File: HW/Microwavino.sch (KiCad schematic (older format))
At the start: 56 parts, among them P1 SMA, P2 SMA, P3 SMA, P4 SMA, U1 MIC5366, U2 MCP1824T, U3 MCP1824T, U4 MCP1824T, U5 ASTXR-12-19.200MHz, U6 MAX2871, U7 Teensy3.2

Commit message: testing connection
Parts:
- added R?: 5.1k, Resistors_SMD:R_0402, symbol R
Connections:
- net 3V3_DIG: now also R?.1
- net CE: now also R?.2
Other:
- note added: "Fast Lock Circuit\n(may be omitted)"
- note added: "Loop Filter"

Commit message: prelim placement
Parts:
- C10, C11, C12, C13, C14, C15, C16, C17, C18, C19, C20, C21, C22, C23, C24, C25, C28, C9: footprint Capacitors_SMD:C_0402 -> VNA:C_0402b
- D1: footprint (none) -> VNA:LED_0603
- R1, R10, R11, R2, R3, R4, R5, R6, R7, R8, R9: footprint Resistors_SMD:R_0402 -> VNA:R_0402b
- R12: renamed from R?; footprint Resistors_SMD:R_0402 -> VNA:R_0402b
- U1: footprint TO_SOT_Packages_SMD:SOT-353_SC-70-5 -> VNA:SOT-23-5
- U7: footprint kicad_teensy-master:Teensy30_31_32_LC -> VNA:Teensy30_31_32_LC_modified
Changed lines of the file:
@@
 F 0 "C12" H 5225 7600 50  0000 L CNN
 F 1 "1u" H 5225 7400 50  0000 L CNN
-F 2 "Capacitors_SMD:C_0402" H 5238 7350 30  0001 C CNN
+F 2 "VNA:C_0402b" H 5238 7350 30  0001 C CNN
 F 3 "" H 5200 7500 60  0000 C CNN
 	1    5200 7500
@@
 F 0 "C10" H 5025 7600 50  0000 L CNN
 F 1 "1u" H 5025 7400 50  0000 L CNN
-F 2 "Capacitors_SMD:C_0402" H 5038 7350 30  0001 C CNN
+F 2 "VNA:C_0402b" H 5038 7350 30  0001 C CNN
 F 3 "" H 5000 7500 60  0000 C CNN
 	1    5000 7500
@@
 F 0 "C9" H 4825 7600 50  0000 L CNN
 F 1 "1u" H 4825 7400 50  0000 L CNN
-F 2 "Capacitors_SMD:C_0402" H 4838 7350 30  0001 C CNN
+F 2 "VNA:C_0402b" H 4838 7350 30  0001 C CNN
 F 3 "" H 4800 7500 60  0000 C CNN
 	1    4800 7500
@@
 F 0 "R1" V 4680 7500 50  0000 C CNN
 F 1 "5.1k" V 4600 7500 50  0000 C CNN
-F 2 "Resistors_SMD:R_0402" V 4530 7500 30  0001 C CNN
+F 2 "VNA:R_0402b" V 4530 7500 30  0001 C CNN
 F 3 "" H 4600 7500 30  0000 C CNN
 	1    4600 7500
@@
 F 0 "C24" H 8725 6950 50  0000 L CNN
 F 1 "820p" H 8725 6750 50  0000 L CNN
-F 2 "Capacitors_SMD:C_0402" H 8738 6700 30  0001 C CNN
+F 2 "VNA:C_0402b" H 8738 6700 30  0001 C CNN
 F 3 "" H 8700 6850 60  0000 C CNN
 	1    8700 6850
@@
 F 0 "R5" V 9130 6700 50  0000 C CNN
 F 1 "240" V 9050 6700 50  0000 C CNN
-F 2 "Resistors_SMD:R_0402" V 8980 6700 30  0001 C CNN
+F 2 "VNA:R_0402b" V 8980 6700 30  0001 C CNN
 F 3 "" H 9050 6700 30  0000 C CNN
 	1    9050 6700
@@
 F 0 "C23" H 8725 6400 50  0000 L CNN
 F 1 "12n" H 8725 6200 50  0000 L CNN
-F 2 "Capacitors_SMD:C_0402" H 8738 6150 30  0001 C CNN
+F 2 "VNA:C_0402b" H 8738 6150 30  0001 C CNN
 F 3 "" H 8700 6300 60  0000 C CNN
 	1    8700 6300
@@
 F 0 "C22" H 8725 6050 50  0000 L CNN
 F 1 "100n" H 8725 5850 50  0000 L CNN
-F 2 "Capacitors_SMD:C_0402" H 8738 5800 30  0001 C CNN
+F 2 "VNA:C_0402b" H 8738 5800 30  0001 C CNN
 F 3 "" H 8700 5950 60  0000 C CNN
 	1    8700 5950
@@
 F 0 "R4" V 8580 5800 50  0000 C CNN
 F 1 "30.1" V 8500 5800 50  0000 C CNN
-F 2 "Resistors_SMD:R_0402" V 8430 5800 30  0001 C CNN
+F 2 "VNA:R_0402b" V 8430 5800 30  0001 C CNN
 F 3 "" H 8500 5800 30  0000 C CNN
 	1    8500 5800
@@
 F 0 "R3" V 8380 5950 50  0000 C CNN
 F 1 "90.9" V 8300 5950 50  0000 C CNN
-F 2 "Resistors_SMD:R_0402" V 8230 5950 30  0001 C CNN
+F 2 "VNA:R_0402b" V 8230 5950 30  0001 C CNN
 F 3 "" H 8300 5950 30  0000 C CNN
 	1    8300 5950
@@
 F 0 "C25" H 10575 6450 50  0000 L CNN
 F 1 "100p" H 10575 6250 50  0000 L CNN
-F 2 "Capacitors_SMD:C_0402" H 10588 6200 30  0001 C CNN
+F 2 "VNA:C_0402b" H 10588 6200 30  0001 C CNN
 F 3 "" H 10550 6350 60  0000 C CNN
 	1    10550 6350
@@
 F 0 "C17" H 5725 4450 50  0000 L CNN
 F 1 "100n" H 5725 4250 50  0000 L CNN
-F 2 "Capacitors_SMD:C_0402" H 5738 4200 30  0001 C CNN
+F 2 "VNA:C_0402b" H 5738 4200 30  0001 C CNN
 F 3 "" H 5700 4350 60  0000 C CNN
 	1    5700 4350
@@
 F 0 "C20" H 5975 4450 50  0000 L CNN
 F 1 "100p" H 5975 4250 50  0000 L CNN
-F 2 "Capacitors_SMD:C_0402" H 5988 4200 30  0001 C CNN
+F 2 "VNA:C_0402b" H 5988 4200 30  0001 C CNN
 F 3 "" H 5950 4350 60  0000 C CNN
 	1    5950 4350
@@
 F 0 "C18" H 5725 5200 50  0000 L CNN
 F 1 "100n" H 5725 5000 50  0000 L CNN
-F 2 "Capacitors_SMD:C_0402" H 5738 4950 30  0001 C CNN
+F 2 "VNA:C_0402b" H 5738 4950 30  0001 C CNN
 F 3 "" H 5700 5100 60  0000 C CNN
 	1    5700 5100
@@
 F 0 "C21" H 5975 5200 50  0000 L CNN
 F 1 "100p" H 5975 5000 50  0000 L CNN
-F 2 "Capacitors_SMD:C_0402" H 5988 4950 30  0001 C CNN
+F 2 "VNA:C_0402b" H 5988 4950 30  0001 C CNN
 F 3 "" H 5950 5100 60  0000 C CNN
 	1    5950 5100
@@
 F 0 "C14" H 5475 4450 50  0000 L CNN
 F 1 "100n" H 5475 4250 50  0000 L CNN
-F 2 "Capacitors_SMD:C_0402" H 5488 4200 30  0001 C CNN
+F 2 "VNA:C_0402b" H 5488 4200 30  0001 C CNN
 F 3 "" H 5450 4350 60  0000 C CNN
 	1    5450 4350
@@
 F 0 "C15" H 5475 5200 50  0000 L CNN
 F 1 "100n" H 5475 5000 50  0000 L CNN
-F 2 "Capacitors_SMD:C_0402" H 5488 4950 30  0001 C CNN
+F 2 "VNA:C_0402b" H 5488 4950 30  0001 C CNN
 F 3 "" H 5450 5100 60  0000 C CNN
 	1    5450 5100
@@
 F 0 "R8" V 11080 6450 50  0000 C CNN
 F 1 "49.9" V 11000 6450 50  0000 C CNN
-F 2 "Resistors_SMD:R_0402" V 10930 6450 30  0001 C CNN
+F 2 "VNA:R_0402b" V 10930 6450 30  0001 C CNN
 F 3 "" H 11000 6450 30  0000 C CNN
 	1    11000 6450
@@
 F 0 "C11" V 5000 6050 50  0000 L CNN
 F 1 "10n" V 5100 6050 50  0000 L CNN
-F 2 "Capacitors_SMD:C_0402" H 5088 5800 30  0001 C CNN
+F 2 "VNA:C_0402b" H 5088 5800 30  0001 C CNN
 F 3 "" H 5050 5950 60  0000 C CNN
 	1    5050 5950
@@
 F 0 "U1" H 3250 5800 60  0000 C CNN
 F 1 "MIC5366" H 3100 6200 60  0000 C CNN
-F 2 "TO_SOT_Packages_SMD:SOT-353_SC-70-5" H 3050 5850 60  0001 C CNN
+F 2 "VNA:SOT-23-5" H 3050 5850 60  0001 C CNN
 F 3 "" H 3050 5850 60  0000 C CNN
 	1    3100 6000
@@
 F 0 "U7" H 11400 4650 60  0000 C CNN
 F 1 "Teensy3.2" H 11400 1650 60  0000 C CNN
-F 2 "kicad_teensy-master:Teensy30_31_32_LC" H 11400 2350 60  0001 C CNN
+F 2 "VNA:Teensy30_31_32_LC_modified" H 11400 2350 60  0001 C CNN
 F 3 "" H 11400 2350 60  0000 C CNN
 	1    11400 3150
@@
 F 0 "C16" H 5725 3650 50  0000 L CNN
 F 1 "100n" H 5725 3450 50  0000 L CNN
-F 2 "Capacitors_SMD:C_0402" H 5738 3400 30  0001 C CNN
+F 2 "VNA:C_0402b" H 5738 3400 30  0001 C CNN
 F 3 "" H 5700 3550 60  0000 C CNN
 	1    5700 3550
@@
 F 0 "C19" H 5975 3650 50  0000 L CNN
 F 1 "100p" H 5975 3450 50  0000 L CNN
-F 2 "Capacitors_SMD:C_0402" H 5988 3400 30  0001 C CNN
+F 2 "VNA:C_0402b" H 5988 3400 30  0001 C CNN
 F 3 "" H 5950 3550 60  0000 C CNN
 	1    5950 3550
@@
 F 0 "C13" H 5475 3650 50  0000 L CNN
 F 1 "100n" H 5475 3450 50  0000 L CNN
-F 2 "Capacitors_SMD:C_0402" H 5488 3400 30  0001 C CNN
+F 2 "VNA:C_0402b" H 5488 3400 30  0001 C CNN
 F 3 "" H 5450 3550 60  0000 C CNN
 	1    5450 3550
@@
 F 0 "R6" V 10880 7100 50  0000 C CNN
 F 1 "49.9" V 10800 7100 50  0000 C CNN
-F 2 "Resistors_SMD:R_0402" V 10730 7100 30  0001 C CNN
+F 2 "VNA:R_0402b" V 10730 7100 30  0001 C CNN
 F 3 "" H 10800 7100 30  0000 C CNN
 	1    10800 7100
@@
 F 0 "C28" H 12475 6450 50  0000 L CNN
 F 1 "100p" H 12475 6250 50  0000 L CNN
-F 2 "Capacitors_SMD:C_0402" H 12488 6200 30  0001 C CNN
+F 2 "VNA:C_0402b" H 12488 6200 30  0001 C CNN
 F 3 "" H 12450 6350 60  0000 C CNN
 	1    12450 6350
@@
 F 0 "R11" V 12980 6450 50  0000 C CNN
 F 1 "49.9" V 12900 6450 50  0000 C CNN
-F 2 "Resistors_SMD:R_0402" V 12830 6450 30  0001 C CNN
+F 2 "VNA:R_0402b" V 12830 6450 30  0001 C CNN
 F 3 "" H 12900 6450 30  0000 C CNN
 	1    12900 6450
@@
 F 0 "R9" V 12780 7100 50  0000 C CNN
 F 1 "49.9" V 12700 7100 50  0000 C CNN
-F 2 "Resistors_SMD:R_0402" V 12630 7100 30  0001 C CNN
+F 2 "VNA:R_0402b" V 12630 7100 30  0001 C CNN
 F 3 "" H 12700 7100 30  0000 C CNN
 	1    12700 7100
@@
 F 0 "R7" V 10880 7800 50  0000 C CNN
 F 1 "49.9" V 10800 7800 50  0000 C CNN
-F 2 "Resistors_SMD:R_0402" V 10730 7800 30  0001 C CNN
+F 2 "VNA:R_0402b" V 10730 7800 30  0001 C CNN
 F 3 "" H 10800 7800 30  0000 C CNN
 	1    10800 7800
@@
 F 0 "R10" V 12780 7800 50  0000 C CNN
 F 1 "49.9" V 12700 7800 50  0000 C CNN
-F 2 "Resistors_SMD:R_0402" V 12630 7800 30  0001 C CNN
+F 2 "VNA:R_0402b" V 12630 7800 30  0001 C CNN
 F 3 "" H 12700 7800 30  0000 C CNN
 	1    12700 7800
@@
 F 0 "D1" H 7400 5525 50  0000 L CNN
 F 1 "LED_Small_ALT" H 7275 5300 50  0001 L CNN
-F 2 "" V 7450 5400 50  0001 C CNN
+F 2 "VNA:LED_0603" V 7450 5400 50  0001 C CNN
 F 3 "" V 7450 5400 50  0001 C CNN
 	1    7450 5400
@@
 F 0 "R2" V 7530 5700 50  0000 C CNN
 F 1 "240" V 7450 5700 50  0000 C CNN
-F 2 "Resistors_SMD:R_0402" V 7380 5700 30  0001 C CNN
+F 2 "VNA:R_0402b" V 7380 5700 30  0001 C CNN
 F 3 "" H 7450 5700 30  0000 C CNN
 	1    7450 5700
@@
 Fast Lock Circuit\n(may be omitted)
 $Comp
-L R R?
+L R R12
 U 1 1 59B1334E
 P 3750 7300
-F 0 "R?" V 3830 7300 50  0000 C CNN
+F 0 "R12" V 3830 7300 50  0000 C CNN
 F 1 "5.1k" V 3750 7300 50  0000 C CNN
-F 2 "Resistors_SMD:R_0402" V 3680 7300 30  0001 C CNN
+F 2 "VNA:R_0402b" V 3680 7300 30  0001 C CNN
 F 3 "" H 3750 7300 30  0000 C CNN
 	1    3750 7300

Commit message: prelim layout
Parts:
- removed C27, C29, C30: 1n, VNA:C_0603b, symbol C
- removed P2, P3, P4: SMA, VNA:CONSMA003.062, symbol SMA
- removed R10: 49.9, VNA:R_0402b, symbol R
- added R13, R14: DNP, VNA:R_0402b, symbol R
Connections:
- net 3V3_IN: now also R13.2
- net 3V3_PLL: now also FB3.2
- net CE: now also U7.7 (5_TX1_PWM); no longer U7.6 (4_RX_PWM)
- net LE: now also U7.6 (4_RX_PWM); no longer U7.7 (5_TX1_PWM)
- net at C8.1, FB3.1, U4.5 (VOUT): now also R14.1
- net at C7.1, FB2.1, U3.5 (VOUT): now also R13.1, R14.2
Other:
- note added: "Coplanar waveguide with GND plane design rules\nOSH park 0.8mm board\ner = 4.6\nw = 0.82 mm\ns = 0.1 mm"

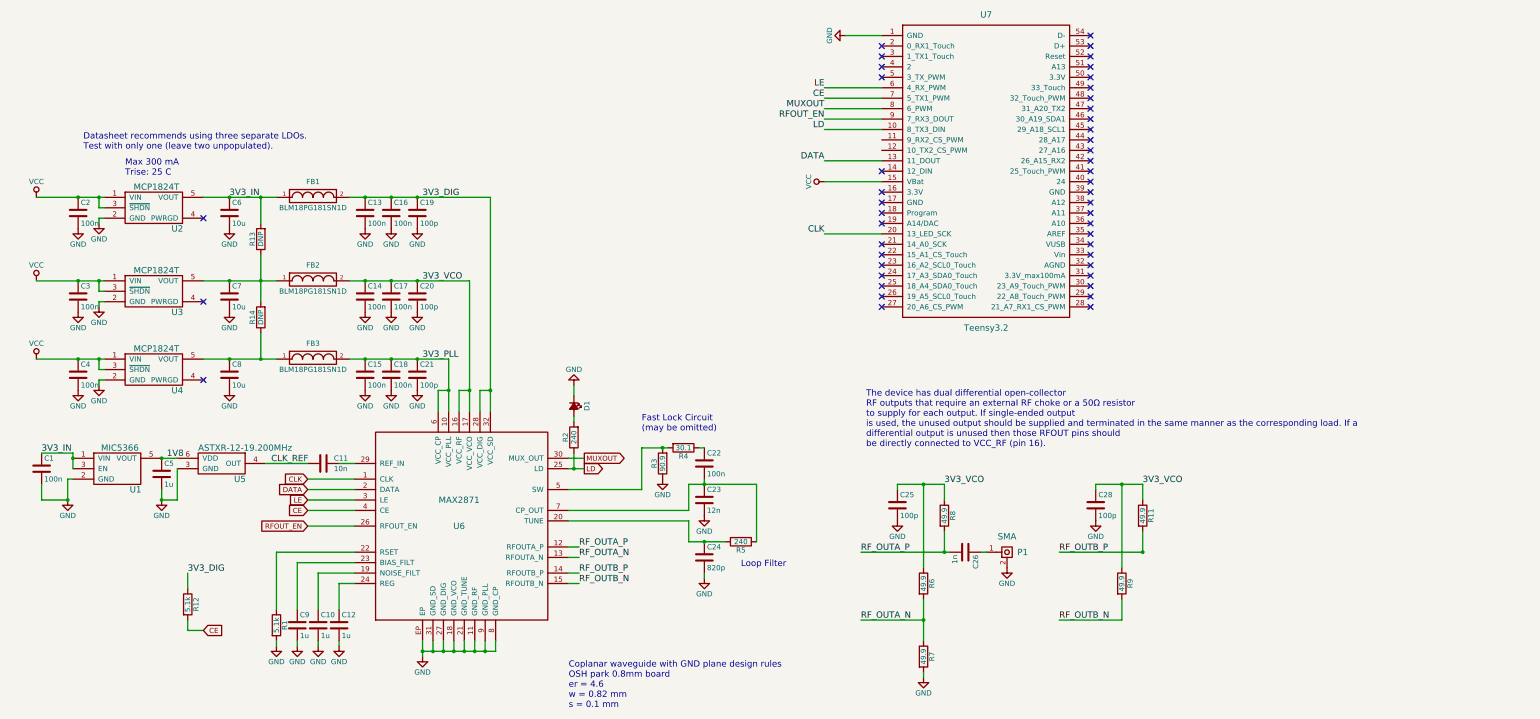
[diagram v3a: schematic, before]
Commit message: route all except power
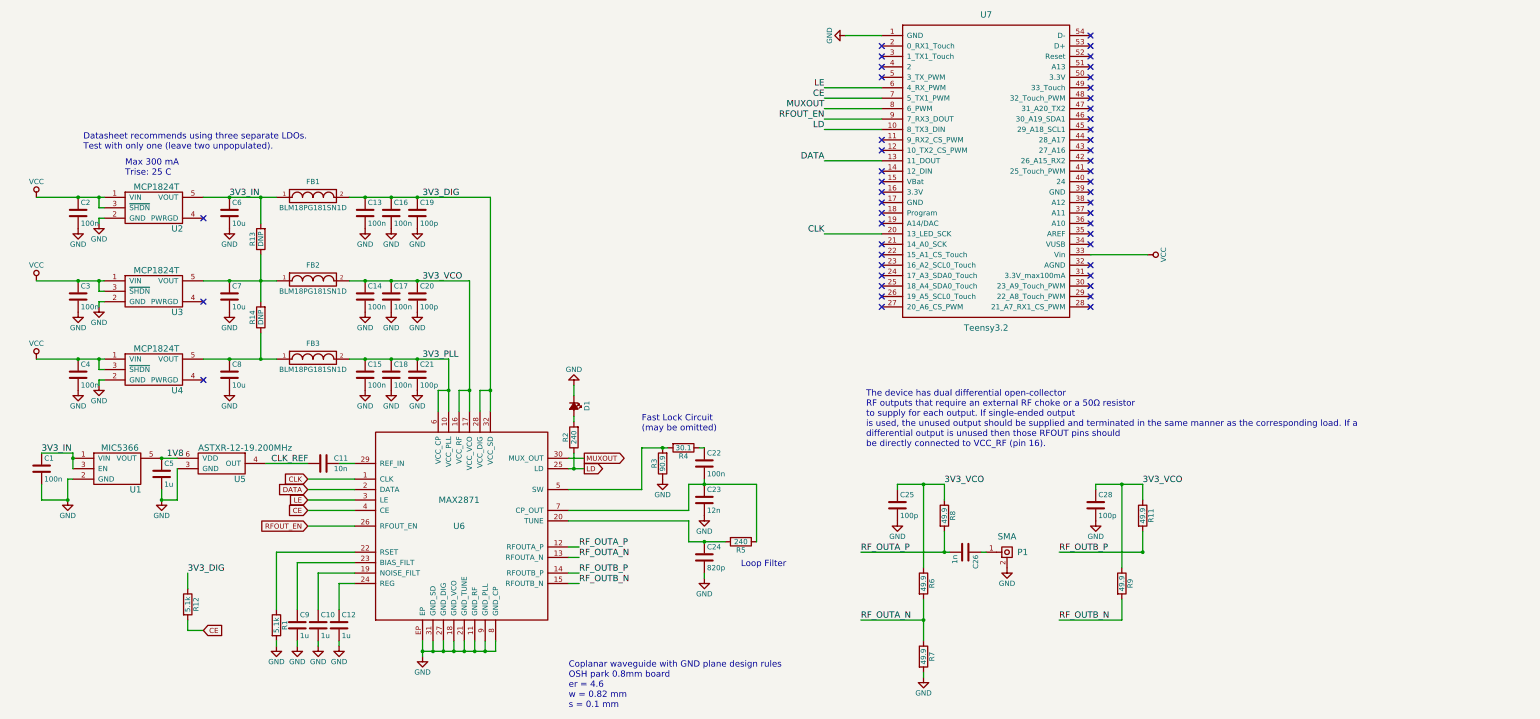
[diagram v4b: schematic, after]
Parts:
- C26: footprint VNA:C_0603b -> VNA:C_0402b
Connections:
- net VCC: now also U7.33 (Vin); no longer U7.15 (VBat)
- no-connect marks 46 -> 48
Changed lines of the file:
@@
 Date "2017-08-29"
 Rev "01"
-Comp "Pero Krivic"
+Comp "Helentronica"
 Comment1 "Microwave synthesizer"
 Comment2 ""
@@
 NoConn ~ 12400 3650
 NoConn ~ 12400 3750
-NoConn ~ 12400 3950
 NoConn ~ 12400 4150
 NoConn ~ 12400 4250
@@
 	4600 6800 4600 7350
 Wire Wire Line
-	6000 7650 6000 7750
-Wire Wire Line
-	6000 7750 6000 7800
-Wire Wire Line
-	6000 7750 6100 7750
-Wire Wire Line
-	6100 7750 6200 7750
-Wire Wire Line
-	6200 7750 6300 7750
-Wire Wire Line
-	6300 7750 6400 7750
-Wire Wire Line
-	6400 7750 6500 7750
-Wire Wire Line
-	6500 7750 6600 7750
-Wire Wire Line
-	6600 7750 6700 7750
+	6000 7650 6000 7800
+Wire Wire Line
+	6000 7750 6700 7750
 Wire Wire Line
 	6100 7750 6100 7650
@@
 	4600 7650 4600 7700
 Wire Wire Line
-	8550 6700 8700 6700
-Wire Wire Line
-	8700 6700 8900 6700
+	8550 6700 8900 6700
 Wire Wire Line
 	8700 7000 8700 7050
 Connection ~ 8700 6700
 Wire Wire Line
-	8550 6150 8700 6150
-Wire Wire Line
-	8700 6150 9200 6150
+	8550 6150 9200 6150
 Wire Wire Line
 	8700 6150 8700 6100
@@
 	8650 5800 8700 5800
 Wire Wire Line
-	8100 5800 8300 5800
-Wire Wire Line
-	8300 5800 8350 5800
+	8100 5800 8350 5800
 Wire Wire Line
 	8100 5800 8100 6200
@@
 	7400 5900 7550 5900
 Wire Wire Line
-	7400 6000 7450 6000
-Wire Wire Line
-	7450 6000 7550 6000
-Wire Wire Line
-	6450 4200 6450 5250
-Wire Wire Line
-	6450 5250 6450 5450
-Wire Wire Line
-	6650 3400 6650 5250
-Wire Wire Line
-	6650 5250 6650 5450
+	7400 6000 7550 6000
+Wire Wire Line
+	6450 4200 6450 5450
+Wire Wire Line
+	6650 3400 6650 5450
 Wire Wire Line
 	6650 5250 6550 5250
 Wire Wire Line
-	6250 4950 6250 5250
-Wire Wire Line
-	6250 5250 6250 5450
+	6250 4950 6250 5450
 Wire Wire Line
 	6150 5250 6150 5450
@@
 	6450 5250 6350 5250
 Wire Wire Line
-	5300 4200 5450 4200
-Wire Wire Line
-	5450 4200 5700 4200
-Wire Wire Line
-	5700 4200 5950 4200
-Wire Wire Line
-	5950 4200 6450 4200
+	5300 4200 6450 4200
 Connection ~ 5950 4200
 Connection ~ 5700 4200
@@
 	2350 5850 2650 5850
 Wire Wire Line
-	2650 5850 2650 5900
-Wire Wire Line
-	2650 5900 2650 6000
+	2650 5850 2650 6000
 Wire Wire Line
 	2600 6300 2600 6100
@@
 	2900 3600 2900 3650
 Wire Wire Line
-	3900 3400 4150 3400
-Wire Wire Line
-	4150 3400 4450 3400
-Wire Wire Line
-	4450 3400 4600 3400
+	3900 3400 4600 3400
 Connection ~ 4150 3400
 Wire Wire Line
@@
 	9850 2750 10400 2750
 Wire Wire Line
-	5300 3400 5450 3400
-Wire Wire Line
-	5450 3400 5700 3400
-Wire Wire Line
-	5700 3400 5950 3400
-Wire Wire Line
-	5950 3400 6650 3400
+	5300 3400 6650 3400
 Connection ~ 5950 3400
 Connection ~ 5700 3400
@@
 	2900 4400 2900 4450
 Wire Wire Line
-	3900 4200 4150 4200
-Wire Wire Line
-	4150 4200 4450 4200
-Wire Wire Line
-	4450 4200 4600 4200
+	3900 4200 4600 4200
 Connection ~ 4150 4200
 Wire Wire Line
@@
 	2900 5150 2900 5200
 Wire Wire Line
-	3900 4950 4150 4950
-Wire Wire Line
-	4150 4950 4450 4950
-Wire Wire Line
-	4450 4950 4600 4950
+	3900 4950 4600 4950
 Connection ~ 4150 4950
 Wire Wire Line
@@
 $EndComp
 Wire Wire Line
-	10200 6800 11000 6800
-Wire Wire Line
-	11000 6800 11050 6800
+	10200 6800 11050 6800
 Text Notes 10250 5800 0    60   ~ 0
 The device has dual differential open-collector \nRF outputs that require an external RF choke or a 50Ω resistor\nto supply for each output. If single-ended output\nis used, the unused output should be supplied and terminated in the same manner as the corresponding load. If a\ndifferential output is unused then those RFOUT pins should\nbe directly connected to VCC_RF (pin 16).
@@
 	10800 6150 10800 6950
 Wire Wire Line
-	10550 6150 10800 6150
-Wire Wire Line
-	10800 6150 11000 6150
+	10550 6150 11000 6150
 Wire Wire Line
 	10550 6150 10550 6200
@@
 Connection ~ 11000 6800
 Wire Wire Line
-	10800 7250 10800 7450
-Wire Wire Line
-	10800 7450 10800 7650
+	10800 7250 10800 7650
 Connection ~ 10800 7450
 $Comp
@@
 $EndComp
 $Comp
-L GND #PWR036
+L GND #PWR035
 U 1 1 59B78EDD
 P 12450 6500
-F 0 "#PWR036" H 12450 6250 50  0001 C CNN
+F 0 "#PWR035" H 12450 6250 50  0001 C CNN
 F 1 "GND" H 12450 6350 50  0000 C CNN
 F 2 "" H 12450 6500 60  0000 C CNN
@@
 	12700 6150 12700 6950
 Wire Wire Line
-	12450 6150 12700 6150
-Wire Wire Line
-	12700 6150 12900 6150
+	12450 6150 12900 6150
 Wire Wire Line
 	12450 6150 12450 6200
 Connection ~ 12700 6150
 Wire Wire Line
-	12900 6800 12900 6600
+	12900 6600 12900 6800
 Connection ~ 12900 6800
 Wire Wire Line
-	12700 7450 12700 7450
+	12100 7450 12700 7450
 $Comp
 L C C26
@@
 F 0 "C26" H 11225 6900 50  0000 L CNN
 F 1 "1n" H 11225 6700 50  0000 L CNN
-F 2 "VNA:C_0603b" H 11238 6650 30  0001 C CNN
+F 2 "VNA:C_0402b" H 11238 6650 30  0001 C CNN
 F 3 "" H 11200 6800 60  0000 C CNN
 	1    11200 6800
@@
 	10800 7950 10800 8000
 $Comp
-L GND #PWR040
+L GND #PWR036
 U 1 1 59B84F12
 P 10800 8000
-F 0 "#PWR040" H 10800 7750 50  0001 C CNN
+F 0 "#PWR036" H 10800 7750 50  0001 C CNN
 F 1 "GND" H 10800 7850 50  0000 C CNN
 F 2 "" H 10800 8000 60  0000 C CNN
@@
 $EndComp
 Wire Wire Line
-	9850 3250 10400 3250
-$Comp
-L VCC #PWR041
+	12950 3950 12400 3950
+$Comp
+L VCC #PWR037
 U 1 1 59B8C676
-P 9850 3250
-F 0 "#PWR041" H 9850 3100 50  0001 C CNN
-F 1 "VCC" H 9850 3400 50  0000 C CNN
-F 2 "" H 9850 3250 50  0001 C CNN
-F 3 "" H 9850 3250 50  0001 C CNN
-	1    9850 3250
-	0    -1   -1   0
+P 12950 3950
+F 0 "#PWR037" H 12950 3800 50  0001 C CNN
+F 1 "VCC" H 12950 4100 50  0000 C CNN
+F 2 "" H 12950 3950 50  0001 C CNN
+F 3 "" H 12950 3950 50  0001 C CNN
+	1    12950 3950
+	0    1    1    0
 $EndComp
 $Comp
@@
 	7450 5300 7450 5200
 $Comp
-L GND #PWR042
+L GND #PWR038
 U 1 1 59B94312
 P 7450 5200
-F 0 "#PWR042" H 7450 4950 50  0001 C CNN
+F 0 "#PWR038" H 7450 4950 50  0001 C CNN
 F 1 "GND" H 7450 5050 50  0000 C CNN
 F 2 "" H 7450 5200 60  0000 C CNN
@@
 Connection ~ 4450 3400
 Wire Wire Line
-	4450 3950 4450 4200
-Wire Wire Line
-	4450 4200 4450 4400
+	4450 3950 4450 4400
 Connection ~ 4450 4200
 Wire Wire Line
@@
 Connection ~ 4450 4950
 Wire Wire Line
-	5300 4950 5450 4950
-Wire Wire Line
-	5450 4950 5700 4950
-Wire Wire Line
-	5700 4950 5950 4950
-Wire Wire Line
-	5950 4950 6250 4950
-Wire Wire Line
-	2300 3400 2700 3400
-Wire Wire Line
-	2700 3400 2900 3400
-Wire Wire Line
-	2900 3400 2950 3400
-Wire Wire Line
-	2300 4200 2700 4200
-Wire Wire Line
-	2700 4200 2900 4200
-Wire Wire Line
-	2900 4200 2950 4200
-Wire Wire Line
-	2300 4950 2700 4950
-Wire Wire Line
-	2700 4950 2900 4950
-Wire Wire Line
-	2900 4950 2950 4950
+	5300 4950 6250 4950
+Wire Wire Line
+	2300 3400 2950 3400
+Wire Wire Line
+	2300 4200 2950 4200
+Wire Wire Line
+	2300 4950 2950 4950
 Text Notes 7400 8300 0    60   ~ 0
 Coplanar waveguide with GND plane design rules\nOSH park 0.8mm board\ner = 4.6\nw = 0.82 mm\ns = 0.1 mm
@@
 	10200 7450 10800 7450
 Wire Wire Line
-	12100 6800 12900 6800
-Wire Wire Line
-	12900 6800 12900 6800
-Wire Wire Line
-	12700 7250 12700 7450
-Wire Wire Line
-	12100 7450 12700 7450
+	12900 6800 12100 6800
+Wire Wire Line
+	12700 7450 12700 7250
+NoConn ~ 10400 2850
+NoConn ~ 10400 2950
+NoConn ~ 10400 3250
 $EndSCHEMATC

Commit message: layout completed v1.0
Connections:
- net 3V3_DIG: no longer R12.1
- net 3V3_PLL: now also R12.1
- net LD: now also D1.2 (A), R2.2, U7.28 (21_A7_RX1_CS_PWM); no longer R2.1, U6.25 (LD), U7.10 (8_TX3_DIN)
- new net: R2.1, U6.25 (LD)
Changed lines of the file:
@@
 Text GLabel 7550 5900 2    49   Output ~ 0
 MUXOUT
-Text GLabel 7550 6000 2    49   Output ~ 0
+Text GLabel 7650 5550 2    49   Output ~ 0
 LD
 $Comp
@@
 Text Label 9850 2350 2    60   ~ 0
 LE
-Text Label 9850 2750 2    60   ~ 0
+Text Label 12950 4450 0    60   ~ 0
 LD
 Text Label 9850 2650 2    60   ~ 0
@@
 NoConn ~ 12400 4250
 NoConn ~ 12400 4350
-NoConn ~ 12400 4450
 NoConn ~ 10400 3150
 NoConn ~ 10400 3350
@@
 	7400 5900 7550 5900
 Wire Wire Line
-	7400 6000 7550 6000
-Wire Wire Line
 	6450 4200 6450 5450
 Wire Wire Line
@@
 	9850 2650 10400 2650
 Wire Wire Line
-	9850 2750 10400 2750
+	12950 4450 12400 4450
 Wire Wire Line
 	5300 3400 6650 3400
@@
 Wire Wire Line
 	7450 5850 7450 6000
-Connection ~ 7450 6000
 Wire Wire Line
 	7450 5300 7450 5200
@@
 	3750 7450 3750 7550
 Text Label 3750 7000 0    60   ~ 0
-3V3_DIG
+3V3_PLL
 Text GLabel 3900 7550 2    49   Input ~ 0
 CE
@@
 NoConn ~ 10400 2950
 NoConn ~ 10400 3250
+NoConn ~ 10400 2750
+Wire Wire Line
+	7450 6000 7400 6000
+Wire Wire Line
+	7450 5550 7650 5550
+Connection ~ 7450 5550
 $EndSCHEMATC
